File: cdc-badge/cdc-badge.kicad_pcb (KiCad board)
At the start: 4 copper layers, 85 x 110 mm, 158 parts, among them J1 USB_C, J2 JST S2B-PH-SM4-TB, J3 Conn_02x20_Odd_Even, J4 Conn_Grove, J5 Conn_02x03_Odd_Even, J6 Conn_01x06, J7 Conn_01x24, Q1 Si1308EDL, Q2 Si1308EDL, SW0 0, SW1 1, SW10 YES, SW11 NO, SW12 power on/reset, SW13 reset, SW14 flash/power off, SW15 MST-22D18G2 3J, SW16 MST-22D18G2 3J, SW2 2, SW3 3, SW4 4, SW5 5, SW6 6, SW7 7, SW8 8, SW9 9, U1 ESP32-S3-WROOM-1-N16R8, U2 TCA9535PWR, U3 TR01-C2P-T301, U5 TLV61070ADBVR, U6 BQ25895RTW, U8 TLV62569DBV

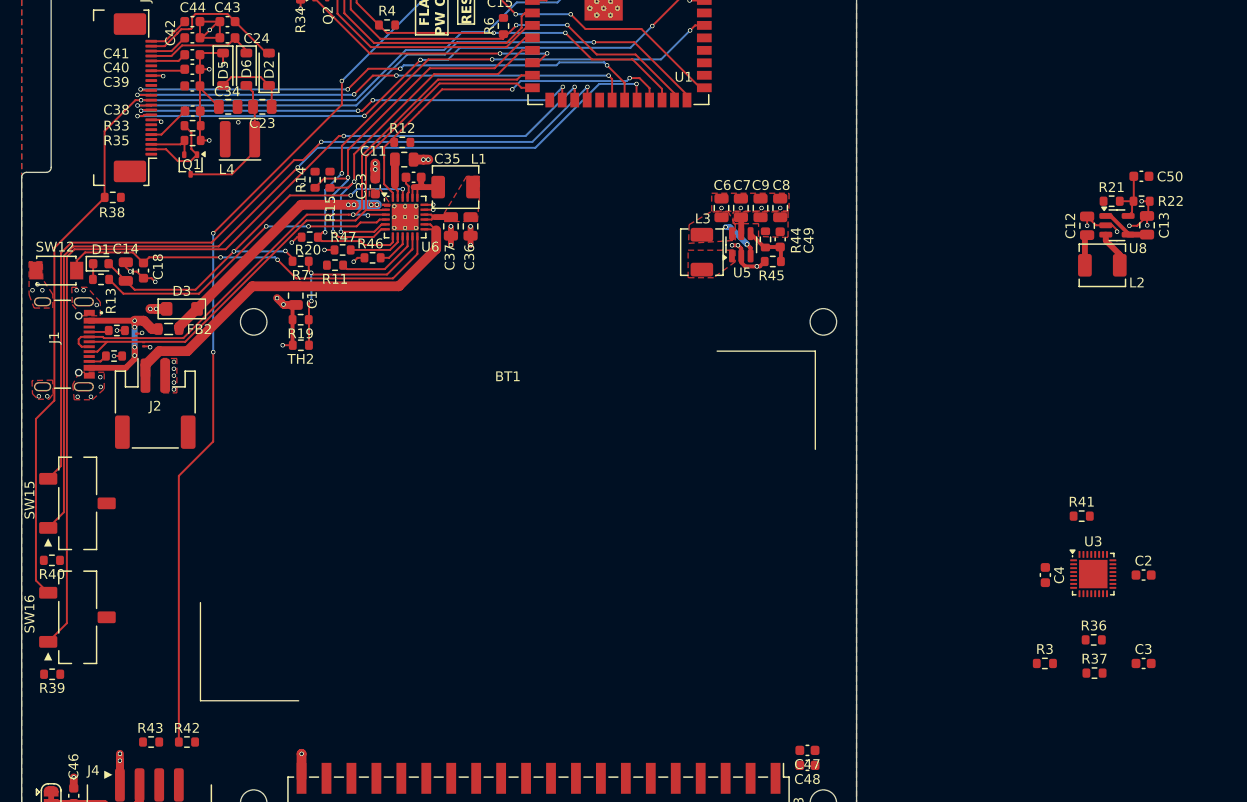
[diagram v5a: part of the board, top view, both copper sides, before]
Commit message: PCB: placement of 3.3V and 5V generators. routing
-placed 3.3V and 5V systems to designated positions
-routing of critical connections between S3 and raspi connector,
optimization of existing routes
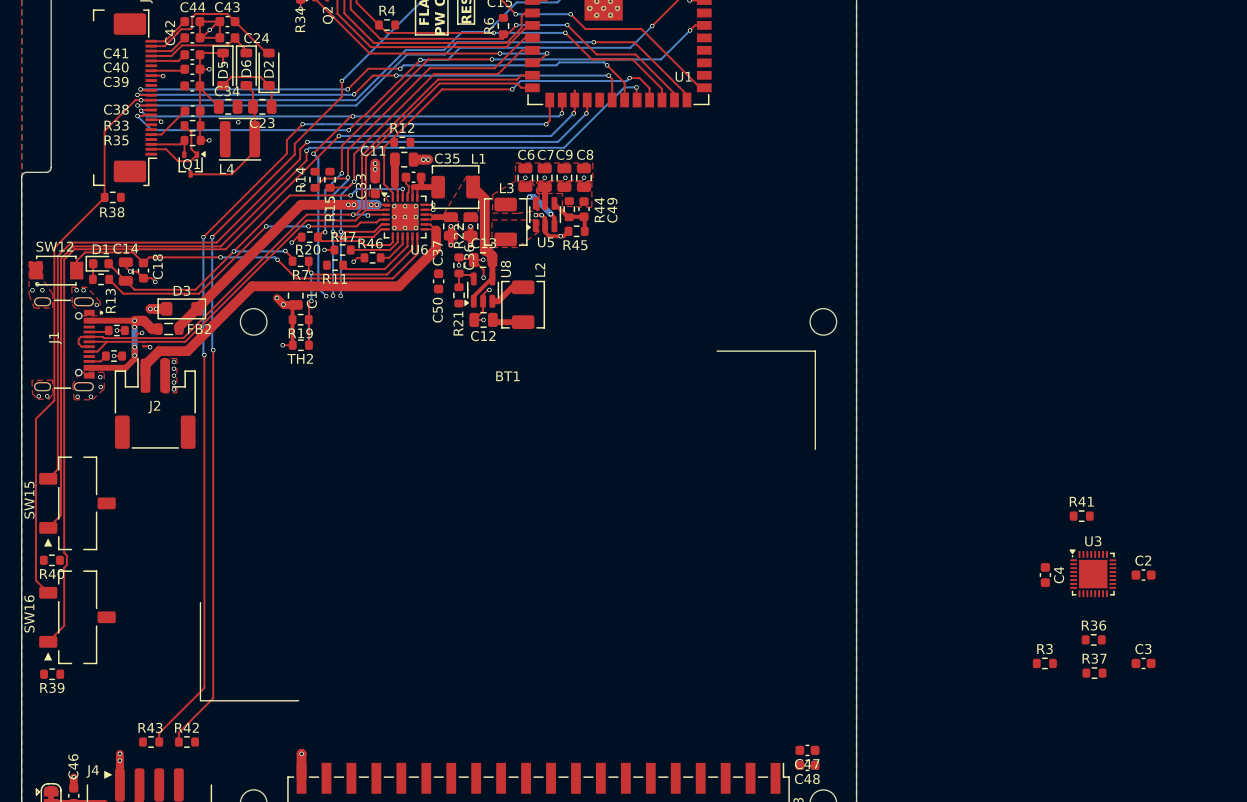
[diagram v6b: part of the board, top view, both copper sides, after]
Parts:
- moved C50 72.3 mm to (97.5, 98.1), turned to 90 degrees
- moved R22 69.8 mm to (99.5, 96.5), turned to 90 degrees
- moved C13 67.7 mm to (102.0, 95.9), turned to 180 degrees
- moved R21 67.1 mm to (99.5, 99.5), turned to 90 degrees
- moved U8 64.9 mm to (102.0, 99.0), turned to 90 degrees
- moved C12 62.2 mm to (102.0, 102.0), turned to 180 degrees
- moved L2 59.1 mm to (106.0, 100.5), turned to -90 degrees
- moved C49 20.2 mm to (112.2, 90.8)
- moved C6 20.2 mm to (106.3, 87.5)
- moved C7 20.2 mm to (108.2, 87.5)
- moved C8 20.2 mm to (112.2, 87.5)
- moved C9 20.2 mm to (110.2, 87.5)
- moved L3 20.2 mm to (104.3, 92.0)
- moved R44 20.2 mm to (110.8, 90.8)
- moved R45 20.2 mm to (111.5, 93.0)
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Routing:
- net /GROVE1: track 0.00 -> 96.4 mm, vias 0 -> 4
- net /SPI_RST_EPD: track 46.4 -> 66.3 mm, vias 4 -> 5
- net VSYS: track 14.2 -> 22.6 mm
- net /I2C0_SCL: track 38.6 -> 45.1 mm, vias 2 -> 3
- net /I2C0_SDA: track 42.2 -> 48.7 mm, vias 2 -> 3
- net Net-(U8-FB): track 5.56 -> 3.05 mm
- net /SPI_BUSY_EPD: track 64.6 -> 65.7 mm
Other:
- board text added: "VBUS ON B.CU FOR VARIANT B"
- board text added: "VERSION A"
- board text added: "VERSION B"

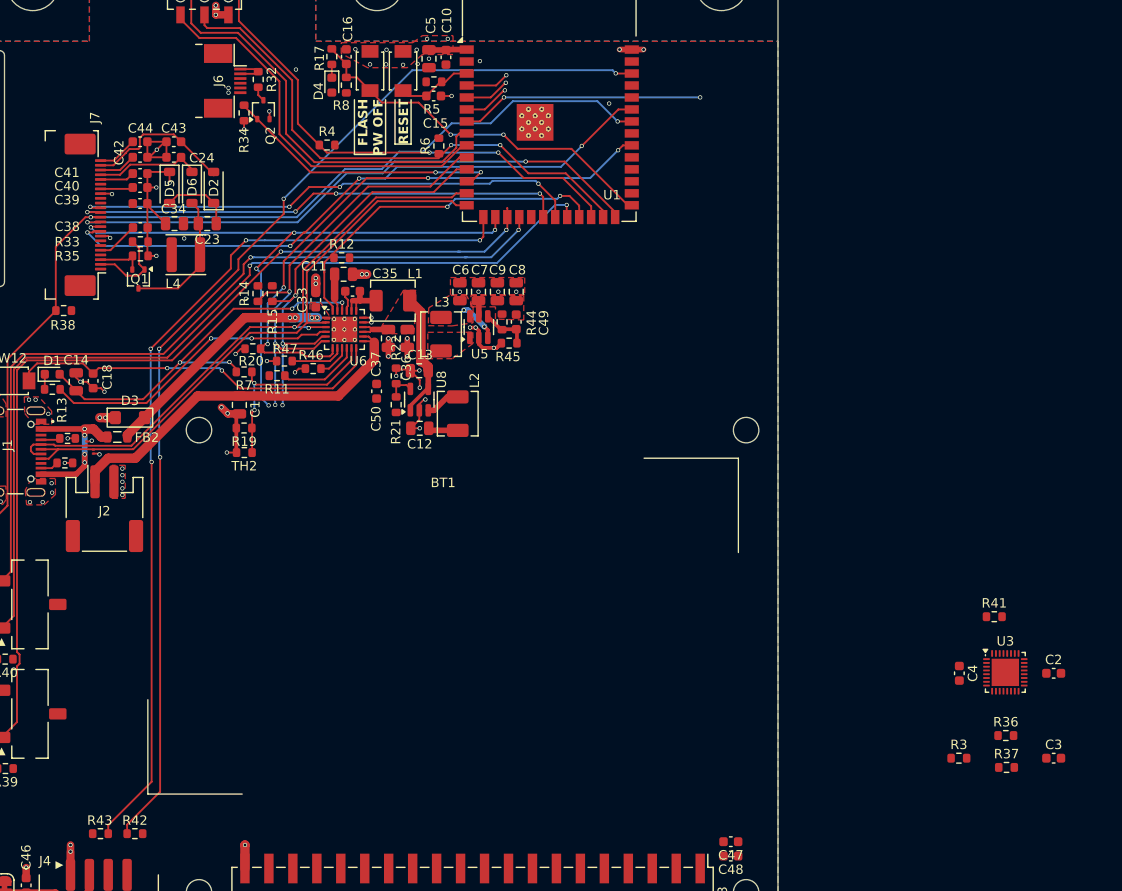
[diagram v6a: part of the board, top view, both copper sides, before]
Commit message: rerouting of several connections between s3 and raspi conn.
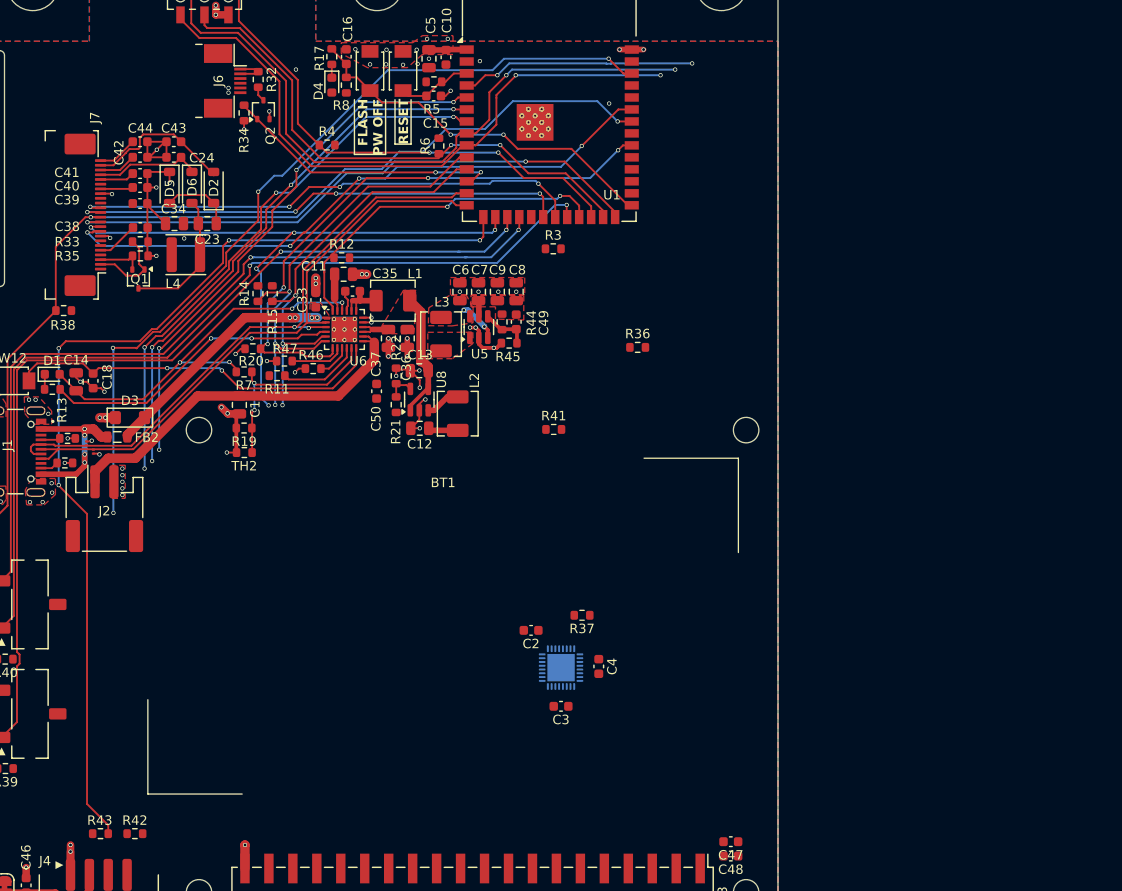
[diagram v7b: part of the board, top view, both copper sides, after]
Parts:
- U3: moved to B.Cu
- moved R3 69.0 mm to (116.2, 83.0)
- moved R36 56.7 mm to (125.1, 93.5)
- moved C2 55.6 mm to (113.8, 123.5), turned to 180 degrees
- moved C3 52.5 mm to (117.0, 131.5), turned to 180 degrees
- moved R41 50.7 mm to (116.2, 102.2)
- moved R37 47.8 mm to (119.2, 121.8), turned to 180 degrees
- moved U3 47.1 mm to (117.0, 127.4), turned to -90 degrees
- moved C4 38.2 mm to (121.0, 127.3)
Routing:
- net /PCM_DIN: track 4.89 -> 57.6 mm, vias 1 -> 4
- net /PCM_FS: track 4.80 -> 57.1 mm, vias 1 -> 4
- net /PCM_DOUT: track 25.8 -> 59.1 mm, vias 2 -> 4
- net /GROVE0: track 116.9 -> 88.5 mm
- net /SAO_GPIO1: track 48.3 -> 74.9 mm, vias 0 -> 2
- net /SAO_GPIO2: track 41.4 -> 66.9 mm, vias 0 -> 2
- net /PCM_CLK: track 4.65 -> 24.9 mm, vias 1 -> 2
- net /GROVE1: track 96.4 -> 106.7 mm
- net /SPI_CS0: track 100.4 -> 99.5 mm
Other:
- board text removed: "3V"
- board text removed: "TR"

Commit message: group the Buttons (and TS01) with components for placement
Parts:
- C19, C20, C21, C22, C25, C26, C27, C28, C29, C30, C31, C32, R10, R16, R18, R23, R24, R25, R26, R27, R28, R29, R30, R31, SW0, SW1, SW10, SW11, SW2, SW3, SW4, SW5, SW6, SW7, SW8, SW9: moved to B.Cu
- moved SW10 262.3 mm to (19.1, 145.0)
- moved SW6 262.1 mm to (19.1, 125.0)
- moved SW9 261.8 mm to (19.1, 135.0)
- moved SW3 254.0 mm to (19.1, 115.0)
- moved R23 253.0 mm to (14.4, 144.0)
- moved C31 252.5 mm to (14.4, 134.0)
- moved C30 252.2 mm to (14.4, 126.0)
- moved R30 248.0 mm to (14.4, 136.0)
- moved SW8 246.3 mm to (35.0, 135.0)
- moved SW0 241.9 mm to (35.0, 145.0)
- moved C29 241.3 mm to (14.4, 116.0)
- moved SW2 238.1 mm to (35.0, 115.0)
- moved SW5 238.1 mm to (35.0, 125.0)
- moved C22 237.8 mm to (14.4, 146.0)
- moved C27 231.4 mm to (30.3, 136.0)
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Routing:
- net GND: track 100.6 -> 98.7 mm, vias 81 -> 80
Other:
- board text added: "1"
- board text added: "2"
- board text added: "3"
